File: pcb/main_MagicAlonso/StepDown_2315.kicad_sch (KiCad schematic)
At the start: 16 parts, among them U6 MP2315

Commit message: schematic and test commit
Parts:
- C17: value 22uF -> 100nF
- R9: value 33k -> 10k
- renumbered R1(1) to Rs1, R1(2) to Rs2
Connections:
- net GND: no longer R9.1
- net at C17.1, U6.7 (VCC): now also R9.2
- net at U6.1 (AAM): now also R9.1; no longer R9.2
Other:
- moved on the sheet: C1, C17, C20, R10, R9

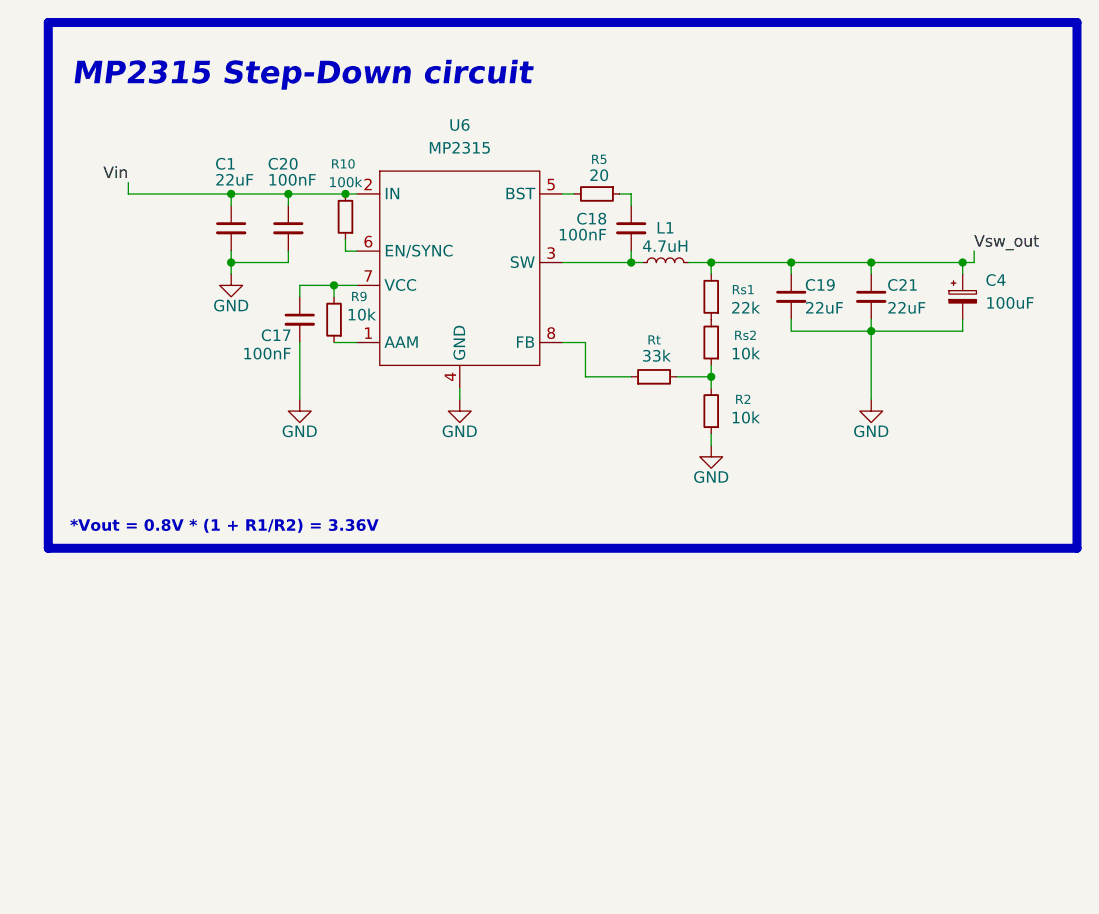
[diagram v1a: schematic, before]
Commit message: Big changes PCB
Advancements on the schematic were made:
- Completed MP2315 circuit
- Passive Buzzer
- Mounting holes & other symbols added

Also the PCB drawings were improved.
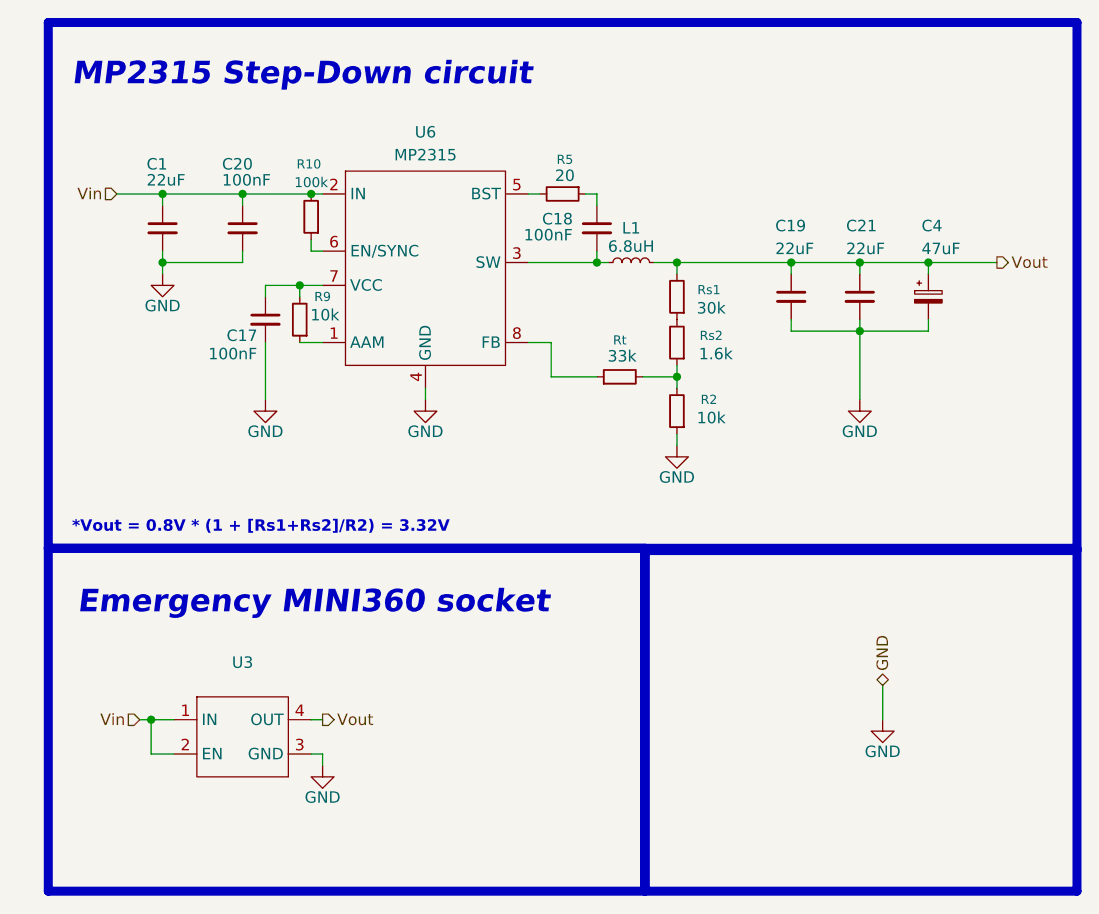
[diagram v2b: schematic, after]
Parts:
- added U3: ~, MixLib:Mix_Mini360-MP4560, symbol MixLib:Mix_Mini360-MP4560
- C4: value 100uF -> 47uF
- L1: value 4.7uH -> 6.8uH
- Rs1: value 22k -> 30k
- Rs2: value 10k -> 1.6k
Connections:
- net GND: now also U3.3 (GND)
- net Vin: now also U3.1 (IN), U3.2 (EN)
- net Vsw_out renamed Vout
- net Vout: now also U3.4 (OUT)
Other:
- note added: "*Vout = 0.8V * (1 + [Rs1+Rs2]/R2) = 3.32V"
- note added: "Emergency MINI360 socket"
- note removed: "*Vout = 0.8V * (1 + R1/R2) = 3.36V"
- moved on the sheet: C1, C17, C18, C20, C21, C4, L1, R10, R2, R5, R9, Rs1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

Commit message: schematic almost finished
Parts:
- added RV1: Pot, symbol Device:R_Potentiometer_Trim
- Rp1: renamed from Rs1; value 30k -> 47k
- Rp2: renamed from Rs2; value 1.6k -> 100k
- U6: renamed from U3; value ~ -> Mini360-MP4560
- renumbered C1 to C17, C20 to C18, C18 to C19, C19 to C20, C4 to C22, C17 to C23, R5 to R14, R10 to R15, R9 to R16, R2 to R17, Rt to Rt1, U6 to U5
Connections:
- net Vout: now also Rp2.2, RV1.3
- net Rt: now reaches Rp1.1
- net Rt: now also R17.2, Rp2.1, Rt1.2, RV1.2; no longer Rp2.2
- no-connect marks 0 -> 1
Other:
- note added: "*Vout = 0.8V * (1 + [Rp1//Rp2]/R2) = 3.34V"
- note added: "Auxiiliary Footprints"
- note added: "GND"
- note removed: "*Vout = 0.8V * (1 + [Rs1+Rs2]/R2) = 3.32V"
- note removed: "Emergency MINI360 socket"
- moved on the sheet: R17, Rp1, Rp2, Rt1, U6

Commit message: some footprint assignment
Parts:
- C17, C18, C19, C20, C21, C23: footprint (none) -> Capacitor_SMD:C_0805_2012Metric
- R14, R15, R16, R17, Rp1, Rp2: footprint (none) -> Resistor_SMD:R_0805_2012Metric
- Rt1: footprint (none) -> Resistor_SMD:R_0603_1608Metric
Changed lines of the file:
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@@
 			)
 		)
-		(property "Footprint" ""
+		(property "Footprint" "Resistor_SMD:R_0805_2012Metric"
 			(at 81.28 44.45 0)
 			(effects
@@
 		)
 		(property "Value" "100k"
-			(at 41.91 30.48 0)
+			(at 41.91 30.226 0)
 			(effects
 				(font
@@
 			)
 		)
-		(property "Footprint" ""
+		(property "Footprint" "Resistor_SMD:R_0805_2012Metric"
 			(at 41.91 34.29 0)
 			(effects
@@
 			)
 		)
-		(property "Footprint" ""
+		(property "Footprint" "Resistor_SMD:R_0805_2012Metric"
 			(at 69.85 31.75 0)
 			(effects
@@
 			)
 		)
-		(property "Footprint" ""
+		(property "Footprint" "Capacitor_SMD:C_0805_2012Metric"
 			(at 95.25 43.18 0)
 			(effects
@@
 			)
 		)
-		(property "Footprint" ""
+		(property "Footprint" "Resistor_SMD:R_0603_1608Metric"
 			(at 76.2 49.53 0)
 			(effects
@@
 			)
 		)
-		(property "Footprint" ""
+		(property "Footprint" "Capacitor_SMD:C_0805_2012Metric"
 			(at 36.83 45.72 0)
 			(effects
@@
 			)
 		)
-		(property "Footprint" ""
+		(property "Footprint" "Capacitor_SMD:C_0805_2012Metric"
 			(at 34.29 35.56 0)
 			(effects
@@
 			)
 		)
-		(property "Footprint" ""
+		(property "Footprint" "Capacitor_SMD:C_0805_2012Metric"
 			(at 73.66 35.56 0)
 			(effects
@@
 			)
 		)
-		(property "Footprint" ""
+		(property "Footprint" "Resistor_SMD:R_0805_2012Metric"
 			(at 82.55 53.34 0)
 			(effects
@@
 			)
 		)
-		(property "Footprint" ""
+		(property "Footprint" "Resistor_SMD:R_0805_2012Metric"
 			(at 83.82 44.45 0)
 			(effects
@@
 			)
 		)
-		(property "Footprint" ""
+		(property "Footprint" "Capacitor_SMD:C_0805_2012Metric"
 			(at 25.4 35.56 0)
 			(effects
@@
 			)
 		)
-		(property "Footprint" ""
+		(property "Footprint" "Capacitor_SMD:C_0805_2012Metric"
 			(at 102.87 43.18 0)
 			(effects
@@
 			)
 		)
-		(property "Footprint" ""
+		(property "Footprint" "Resistor_SMD:R_0805_2012Metric"
 			(at 40.64 45.72 0)
 			(effects

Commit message: footprint assingment completed
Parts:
- C22: footprint (none) -> Connector_JST:JST_XH_B2B-XH-A_1x02_P2.50mm_Vertical
- L1: footprint (none) -> Inductor_SMD:L_TDK_SLF6025
- RV1: footprint (none) -> Potentiometer_SMD:Potentiometer_Vishay_TS53YJ_Vertical
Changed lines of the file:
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@@
 			)
 		)
-		(property "Footprint" ""
+		(property "Footprint" "Connector_JST:JST_XH_B2B-XH-A_1x02_P2.50mm_Vertical"
 			(at 110.49 43.18 0)
 			(effects
@@
 			)
 		)
-		(property "Footprint" ""
+		(property "Footprint" "Inductor_SMD:L_TDK_SLF6025"
 			(at 77.47 39.37 0)
 			(effects
@@
 			)
 		)
-		(property "Footprint" ""
+		(property "Footprint" "Potentiometer_SMD:Potentiometer_Vishay_TS53YJ_Vertical"
 			(at 63.5 92.71 0)
 			(effects

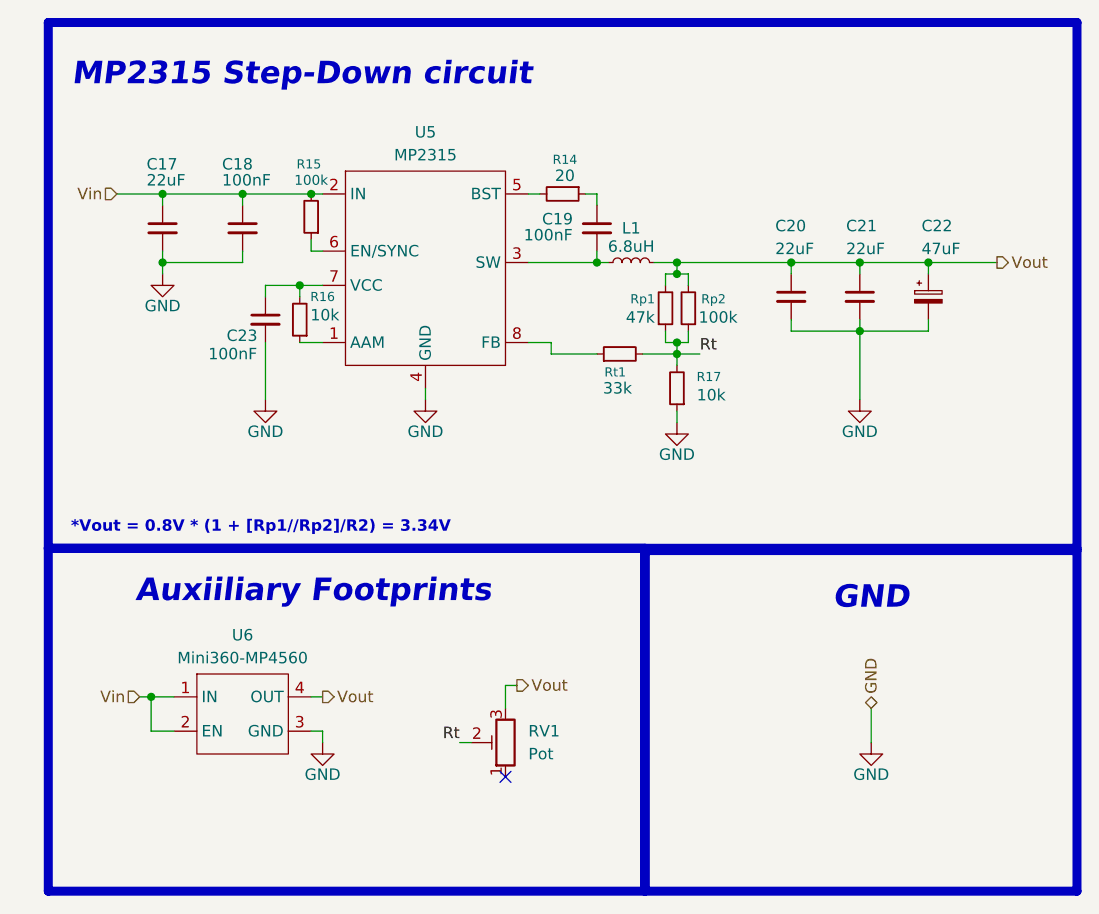
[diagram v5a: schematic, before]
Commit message: pcb components & label fixes
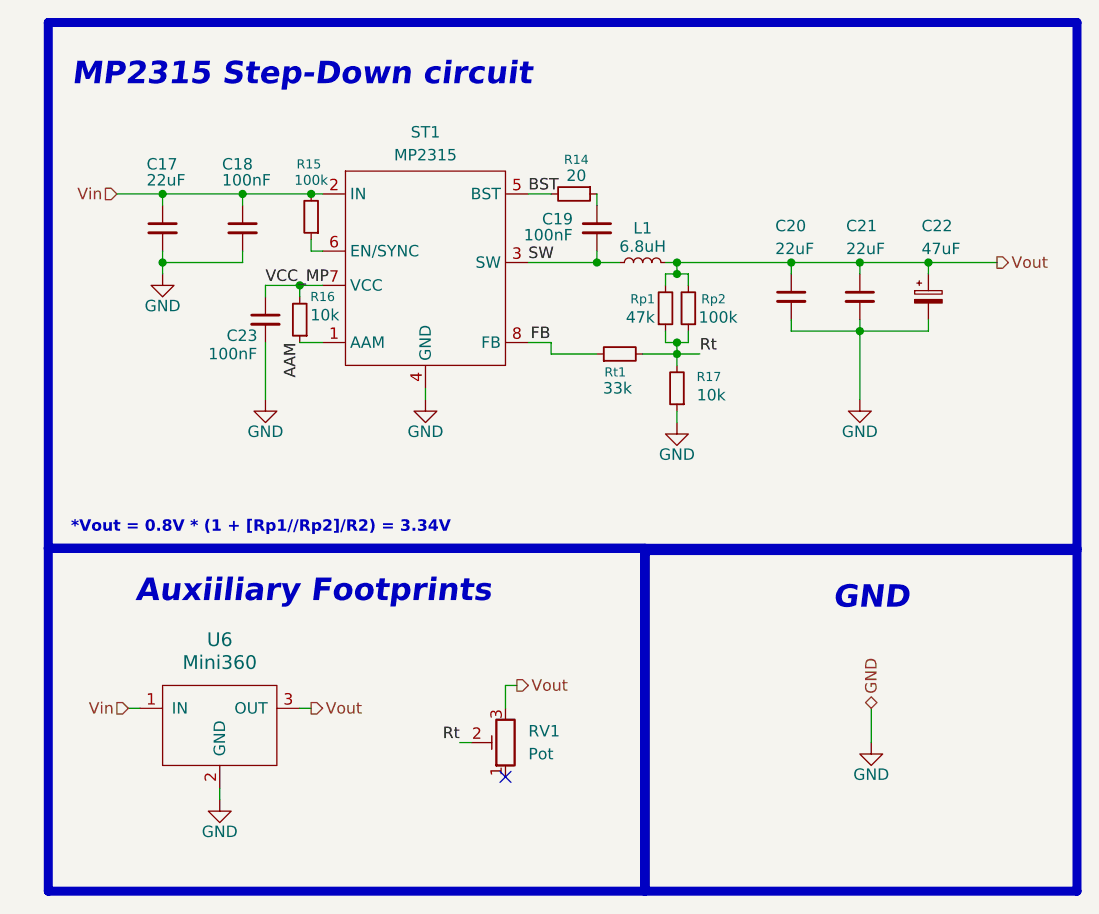
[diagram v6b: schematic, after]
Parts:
- removed U6: Mini360-MP4560, MixLib:Mix_Mini360-MP4560, symbol MixLib:Mix_Mini360-MP4560
- added U6: Mini360, MixLib:Mini360_step-down, symbol MixLib:Mini360
- C22: footprint Connector_JST:JST_XH_B2B-XH-A_1x02_P2.50mm_Vertical -> Capacitor_SMD:CP_Elec_6.3x5.4
- renumbered U5 to ST1
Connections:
- net GND: now also U6.2 (GND)
- net Vin: now also U6.1 (IN)
- net Vout: now also U6.3 (OUT)
- net BST: now reaches R14.2, ST1.5 (BST)
- net FB: now reaches Rt1.1, ST1.8 (FB)
- net VCC_MP: now reaches C23.1, R16.2, ST1.7 (VCC)
- net SW: now reaches C19.2, L1.1, ST1.3 (SW)
- net AAM: now reaches R16.1, ST1.1 (AAM)
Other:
- moved on the sheet: L1, R14

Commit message: more pcb stuff ha
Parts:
- removed C22: 47uF, Capacitor_SMD:CP_Elec_6.3x5.4, symbol Device:C_Polarized_Small
- added C22: 22uF, Capacitor_SMD:C_0805_2012Metric, symbol Device:C_Small
- C18, C19, C23: footprint Capacitor_SMD:C_0805_2012Metric -> Capacitor_SMD:C_0603_1608Metric
- R15, R16: footprint Resistor_SMD:R_0805_2012Metric -> Resistor_SMD:R_0603_1608Metric
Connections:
- net GND: now also C22.2
- net Vout: now also C22.1
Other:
- note removed: "GND"
- moved on the sheet: C20
